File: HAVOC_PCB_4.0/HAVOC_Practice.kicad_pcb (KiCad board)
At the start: 2 copper layers, 90 x 100 mm, 47 parts, among them J10 BATT/switch, J3 NG, J7 solenoid, J8 Micro_SD_Card, J9 BNO, Q1 NMOS, Q2 NMOS, Q3 NMOS, Q4 NMOS, Q5 NMOS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

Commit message: test branch
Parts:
- added J1: 132134, SHC:AMPHENOL_132134_SMA, F.Cu at (26.7, 104.5)
- D5, D9, J3: footprint SHC:CONN4_S4B-XH_JST=SMD4pin -> Connector_Molex:Molex_Mini-Fit_Jr_5569-04A2_2x02_P4.20mm_Horizontal
- J10, J7, J9: footprint SHC:CONN4_S4B-XH_JST=SMD4pin -> Connector_Molex:Molex_Mini-Fit_Jr_5569-04A2_2x02_P4.20mm_Horizontal; moved to B.Cu
- Q7, Q8, R1, R2, R3, R5: moved to F.Cu
- moved Q4 80.9 mm to (183.0, 51.8)
- moved Q3 80.9 mm to (183.0, 47.8)
- moved Q5 80.9 mm to (183.0, 56.0)
- moved R10 80.9 mm to (179.8, 47.8)
- moved R11 80.9 mm to (179.8, 51.8)
- moved R13 80.9 mm to (179.8, 56.0)
- moved U6 78.7 mm to (167.7, 86.5), turned to 90 degrees
- moved Q1 77.8 mm to (179.5, 145.5)
- moved Q2 77.8 mm to (179.5, 141.5)
- moved Q6 77.8 mm to (177.5, 143.8)
- moved R4 77.8 mm to (173.5, 143.8)
- moved R8 77.8 mm to (175.5, 141.5)
- moved R9 77.8 mm to (175.7, 145.5)
- moved D5 48.3 mm to (113.7, 69.6)
- moved R5 33.9 mm to (101.2, 35.1), turned to 90 degrees
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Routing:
- net +5V: track 185.4 -> 0.00 mm, vias 4 -> 0
- net +3V3: track 114.1 -> 0.00 mm, vias 2 -> 0
- net /SDA: track 81.1 -> 0.00 mm, vias 1 -> 0
- net /SCL: track 76.2 -> 0.00 mm, vias 1 -> 0
- net /MISO: track 66.7 -> 0.00 mm
- net /PWM1: track 64.6 -> 0.00 mm, vias 3 -> 0
- net /side_LED: track 63.4 -> 0.00 mm, vias 2 -> 0
- net /MOSI: track 61.7 -> 0.00 mm
- net /VUSB: track 60.2 -> 0.00 mm
- net /PWM2: track 59.7 -> 0.00 mm, vias 3 -> 0
- net /CS: track 59.3 -> 0.00 mm
- net /VIN: track 52.7 -> 0.00 mm
- net /SCLK: track 49.4 -> 0.00 mm
- net /green: track 37.8 -> 0.00 mm
- net /blue: track 26.0 -> 0.00 mm
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- removed copper zone on F.Cu, net +12V
- removed copper zone on F.Cu, net +BATT
- removed copper zone on B.Cu, net GND
- removed copper zone on F.Cu, net GND
- removed copper zone on F.Cu, net Net-(D1-A)
- removed copper zone on F.Cu, net Net-(J10-Pin_2)
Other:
- board text removed: "+12V"
- board text removed: "+12v"
- board text removed: "Batt+"
- board text removed: "Batt-"
- board text removed: "Batt/SW"
- board text removed: "Pow"
- board text removed: "RGBLED"
- board text removed: "SDN"
- board text removed: "SW"
- board text removed: "side LED"
- board text removed: "solenoid"

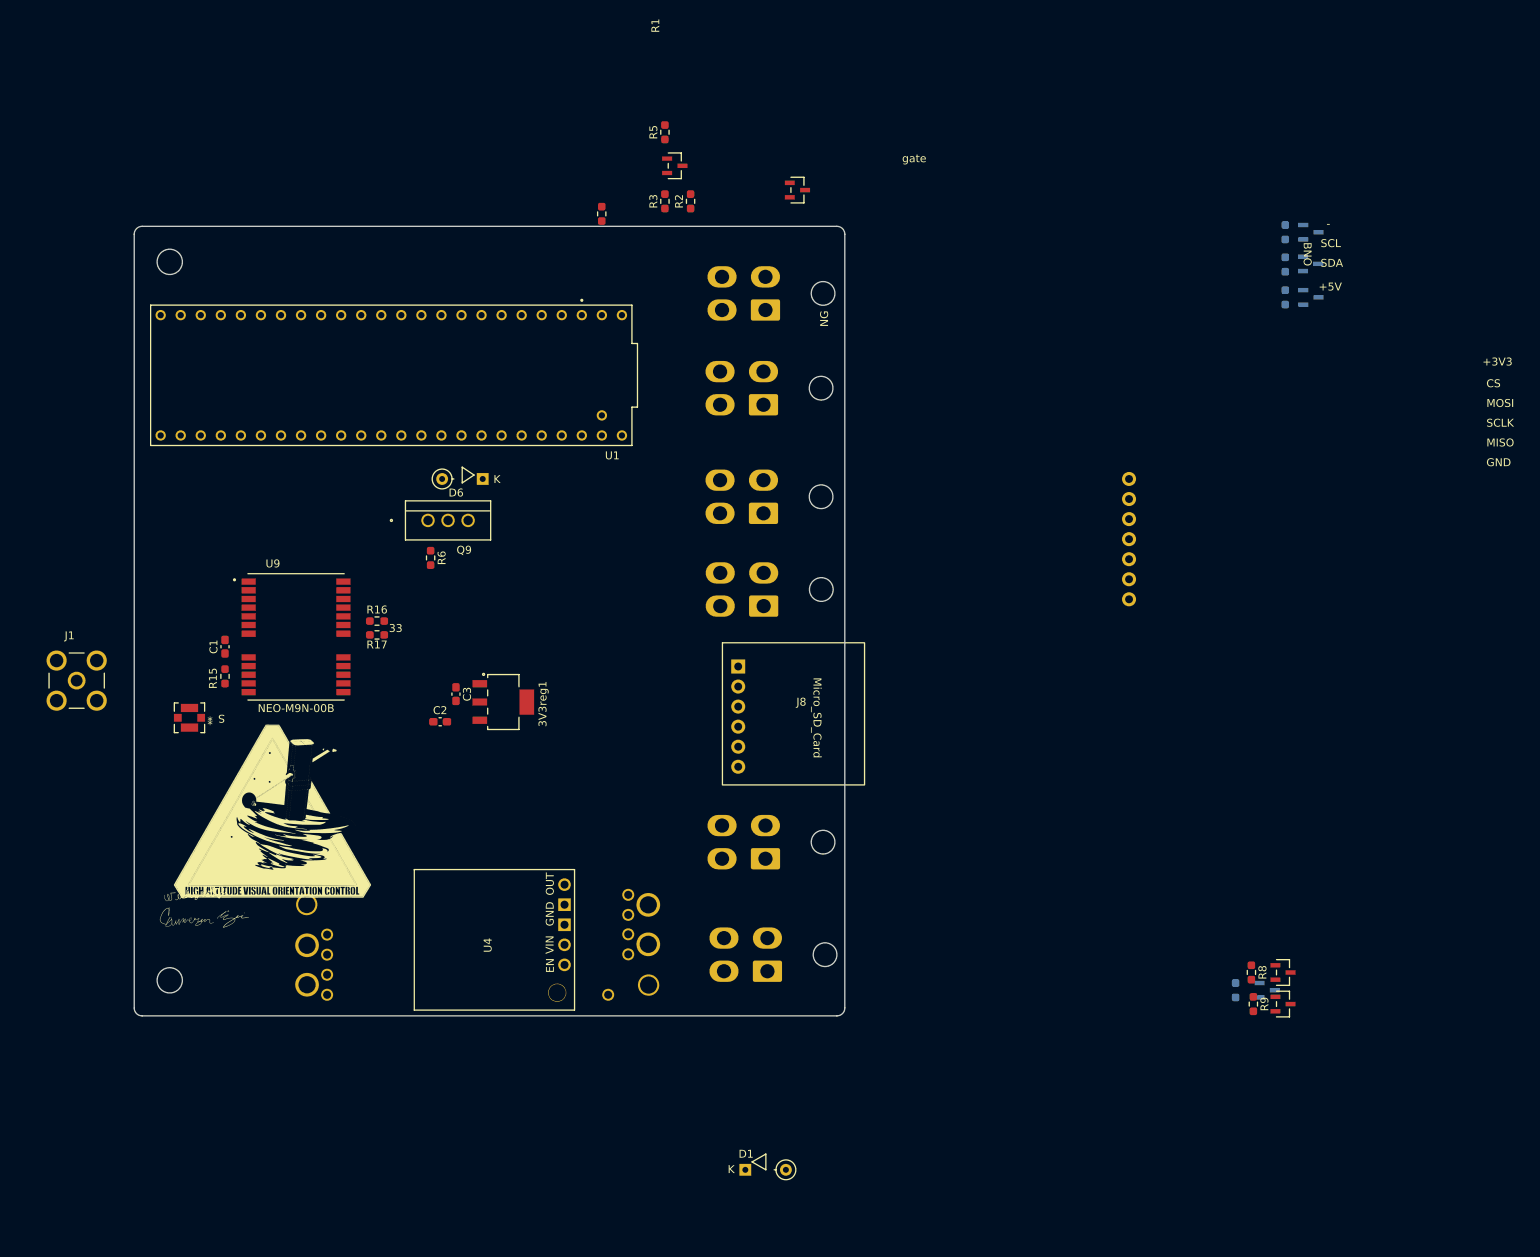
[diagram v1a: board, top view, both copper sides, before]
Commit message: wiring new connectors
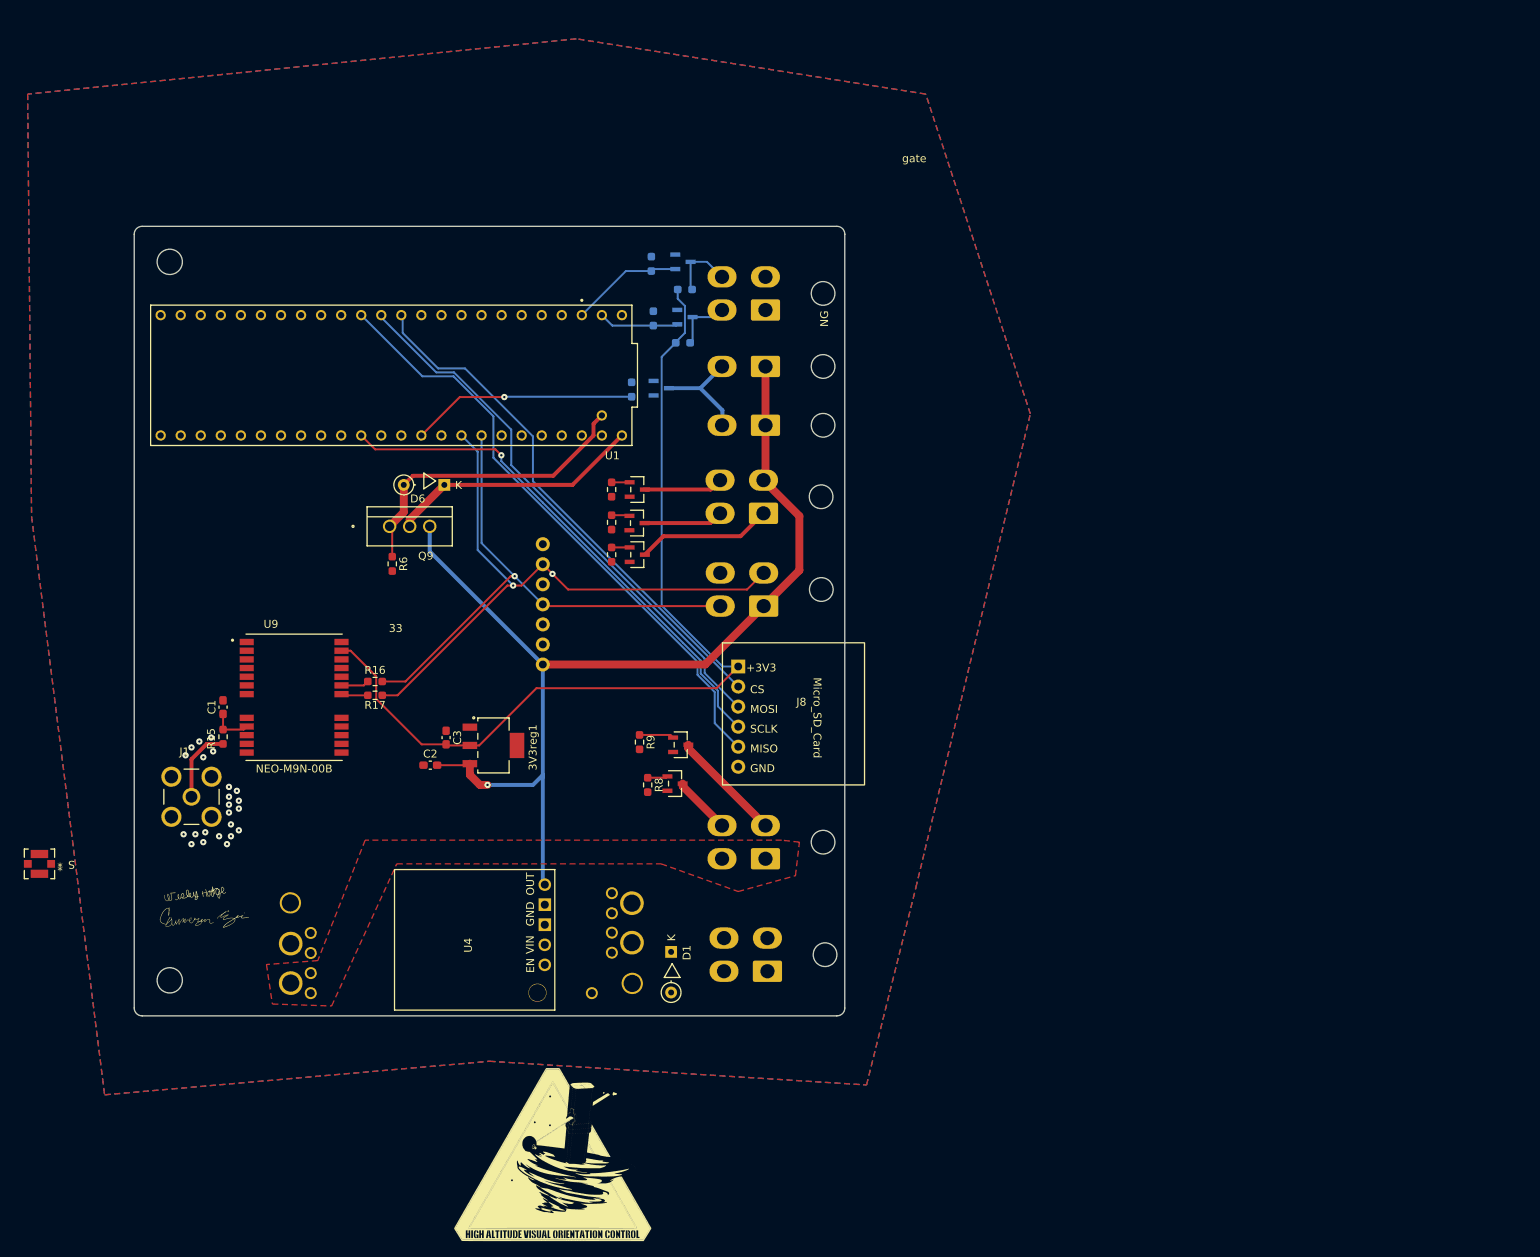
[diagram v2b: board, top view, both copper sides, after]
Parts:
- removed D5: LED_Dual_AAKK, Connector_Molex:Molex_Mini-Fit_Jr_5569-04A2_2x02_P4.20mm_Horizontal
- added D2: LED, Connector_Molex:Molex_Mini-Fit_Jr_5569-02A2_2x01_P4.20mm_Horizontal, B.Cu at (114.0, 72.2)
- added D3: LED, Connector_Molex:Molex_Mini-Fit_Jr_5569-02A2_2x01_P4.20mm_Horizontal, B.Cu at (114.0, 64.8)
- Q3, Q4, Q5, R10, R11, R13: moved to F.Cu
- Q7, Q8, R1, R2, R3, R5: moved to B.Cu
- moved Q6 108.2 mm to (100.8, 67.5)
- moved R4 107.9 mm to (97.0, 67.7)
- moved Q3 94.6 mm to (97.7, 88.6), turned to -90 degrees
- moved R10 94.6 mm to (94.5, 88.6), turned to -90 degrees
- moved Q4 91.4 mm to (97.7, 84.6), turned to -90 degrees
- moved R11 91.4 mm to (94.5, 84.5), turned to -90 degrees
- moved Q5 88.7 mm to (97.7, 80.3), turned to -90 degrees
- moved R13 88.7 mm to (94.5, 80.3), turned to -90 degrees
- moved R9 84.5 mm to (98.0, 112.3)
- moved Q1 83.1 mm to (103.2, 112.7)
- moved Q2 80.6 mm to (102.5, 117.6)
- moved R8 80.1 mm to (99.0, 117.8)
- moved U6 74.7 mm to (93.4, 94.8)
- moved G*** 56.1 mm to (87.0, 165.0)
- moved D1 27.7 mm to (102.0, 141.5), turned to -90 degrees
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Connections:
- D9 pad 1: +5V -> Net-(D9-RK)
- D9 pad 2: Net-(D9-RK) -> +5V
- J7 pad 2: +12V -> Net-(J7-Pin_2)
- J7 pad 3: Net-(J7-Pin_3) -> +12V
- Q1 pad 1: Net-(J7-Pin_3) -> Net-(J7-Pin_2)
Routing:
- net +5V: track 0.00 -> 132.6 mm, vias 0 -> 1
- net +3V3: track 0.00 -> 115.6 mm
- net /SDA: track 0.00 -> 79.1 mm, vias 0 -> 2
- net /MISO: track 0.00 -> 76.7 mm
- net /MOSI: track 0.00 -> 69.6 mm
- net /SCL: track 0.00 -> 69.5 mm, vias 0 -> 1
- net /CS: track 0.00 -> 66.7 mm
- net /SCLK: track 0.00 -> 65.6 mm, vias 0 -> 1
- net /VUSB: track 0.00 -> 39.6 mm
- net /VIN: track 0.00 -> 32.2 mm
- net /side_LED: track 0.00 -> 28.7 mm, vias 0 -> 1
- net Net-(D9-RK): track 0.00 -> 18.5 mm
- net Net-(J7-Pin_2): track 0.00 -> 14.3 mm
- net /SDN: track 0.00 -> 14.3 mm
- net Net-(D2-K): track 0.00 -> 13.8 mm
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- added copper zone on F.Cu, net +12V
- added copper zone on B.Cu, net GND
- added copper zone on F.Cu, net GND
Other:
- board text removed: "+5V"
- board text removed: "SCL"
- board text removed: "SDA"
- board text removed: "control"

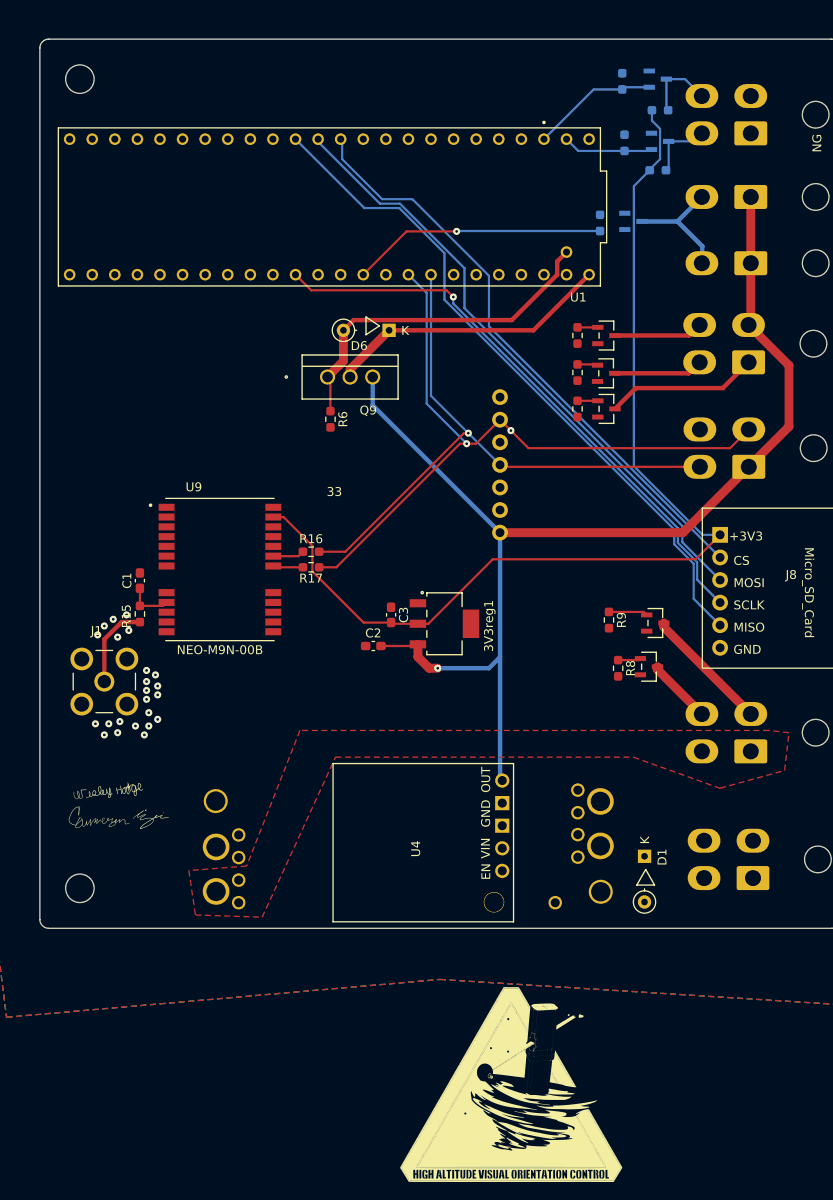
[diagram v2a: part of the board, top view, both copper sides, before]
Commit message: adding traces, still needs solenoid traces mich have to change pins
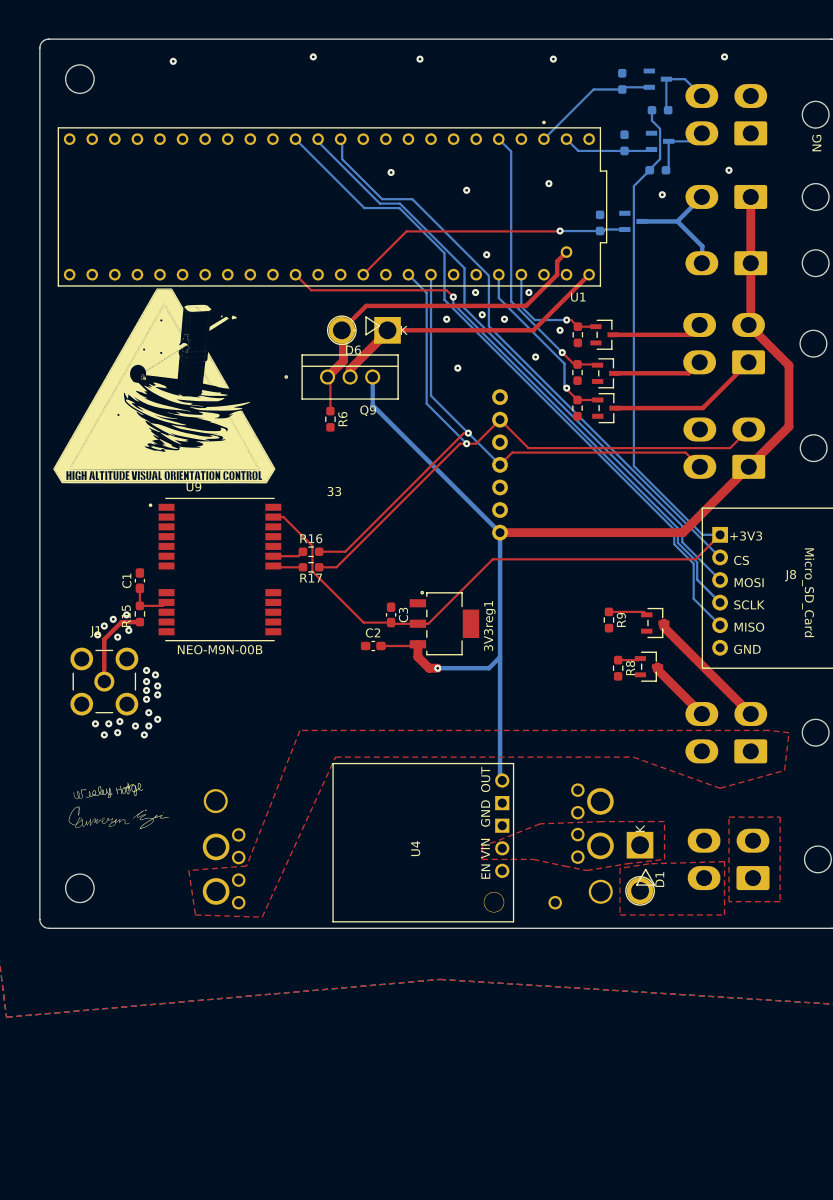
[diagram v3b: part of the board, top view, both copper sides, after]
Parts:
- moved G*** 87.7 mm to (48.0, 86.4)
- moved Q3 8.34 mm to (97.5, 80.2)
- moved R10 8.34 mm to (94.5, 80.2)
- moved Q5 8.16 mm to (97.7, 88.5)
- moved R13 8.16 mm to (94.5, 88.5)
- moved D1 1.35 mm to (101.5, 140.2)
- moved D6 0.18 mm to (70.5, 79.8)
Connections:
- D9 pad 1: Net-(D9-RK) -> Net-(D9-BK)
- D9 pad 4: Net-(D9-BK) -> Net-(D9-RK)
- J10 pad 1: Net-(D1-A) -> Net-(J10-Pin_2)
- J10 pad 3: Net-(J10-Pin_2) -> Net-(D1-A)
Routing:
- net /green: track 2.29 -> 31.8 mm, vias 0 -> 1
- net /blue: track 2.29 -> 20.1 mm, vias 0 -> 1
- net /red: track 2.29 -> 12.9 mm, vias 0 -> 1
- net Net-(D9-BK): track 10.0 -> 18.5 mm
- net Net-(D9-RK): track 18.5 -> 10.2 mm
- net /side_LED: track 28.7 -> 31.5 mm
- net /SCL: track 69.5 -> 70.6 mm
- net /SDA: vias 2 -> 1
- net GND: vias 23 -> 42
- added copper zone on F.Cu, net +BATT
- added copper zone on F.Cu, net Net-(D1-A)
- added copper zone on F.Cu, net Net-(J10-Pin_2)
